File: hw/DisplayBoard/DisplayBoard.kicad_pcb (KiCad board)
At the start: 2 copper layers, 71.1 x 50.8 mm, 21 parts, among them Q1 2N3906, Q2 2N3906, Q3 2N3906, Q4 2N3906, U1 CA56-12EWA

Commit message: routed all traces
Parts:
- added J1: Conn_02x08_Odd_Even, Pin_Headers:Pin_Header_Straight_2x08_Pitch2.54mm, F.Cu at (58.4, 97.2)
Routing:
- net /AN3: track 0.00 -> 44.7 mm, vias 0 -> 1
- net Net-(R2-Pad1): track 0.00 -> 43.9 mm
- net /AN2: track 0.00 -> 43.2 mm, vias 0 -> 1
- net /AN1: track 0.00 -> 41.4 mm, vias 0 -> 1
- net /AN0: track 0.00 -> 39.8 mm
- net /VCC3: track 0.00 -> 39.5 mm
- net Net-(R1-Pad1): track 0.00 -> 39.4 mm
- net /VCC2: track 0.00 -> 38.2 mm
- net /VCC1: track 0.00 -> 35.2 mm
- net /VCC0: track 0.00 -> 31.5 mm
- net Net-(Q1-Pad3): track 0.00 -> 30.6 mm
- net Net-(R6-Pad1): track 0.00 -> 30.5 mm, vias 0 -> 1
- net Net-(Q3-Pad3): track 0.00 -> 30.1 mm
- net Net-(Q4-Pad3): track 0.00 -> 28.7 mm
- net Net-(R3-Pad1): track 0.00 -> 28.0 mm
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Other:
- board text added: "HexClock display board 0.1 11-May-2019 https://github.com/daveho/HexClock"

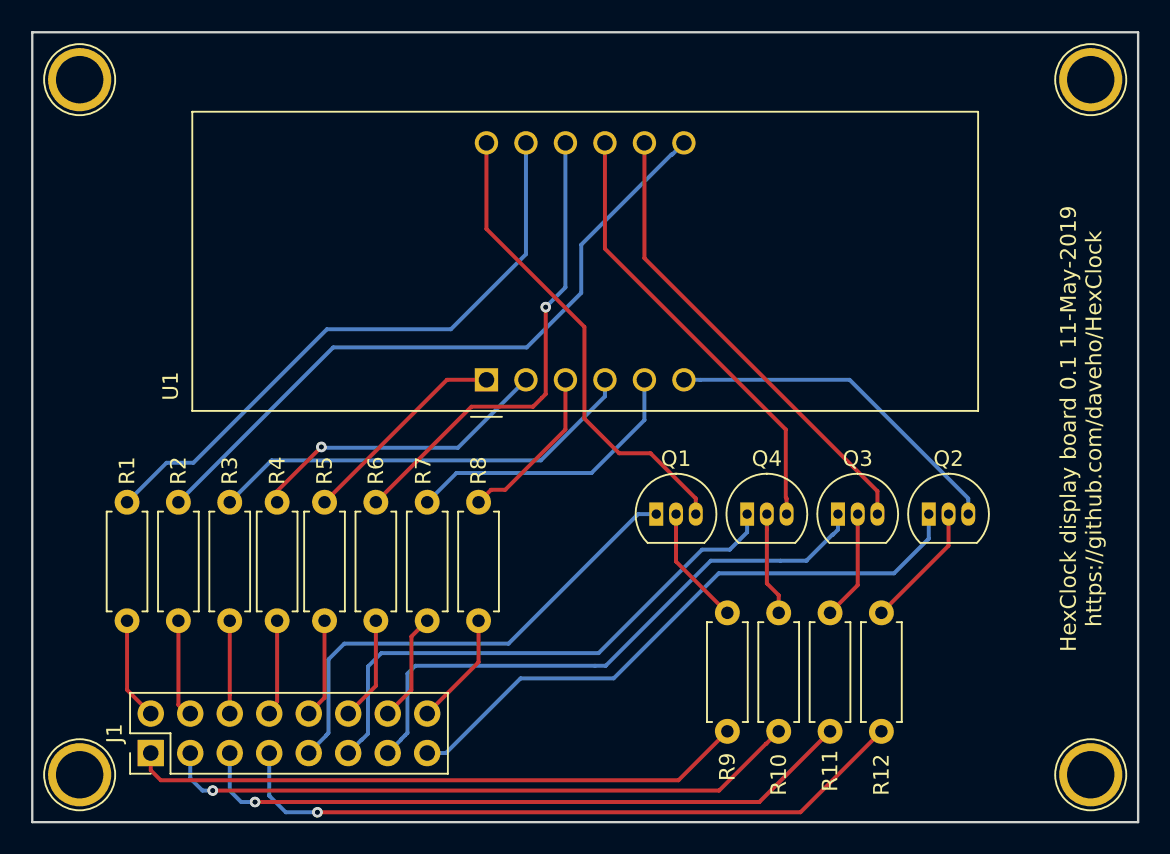
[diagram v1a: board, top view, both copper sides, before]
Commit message: copper pours on both copper layers
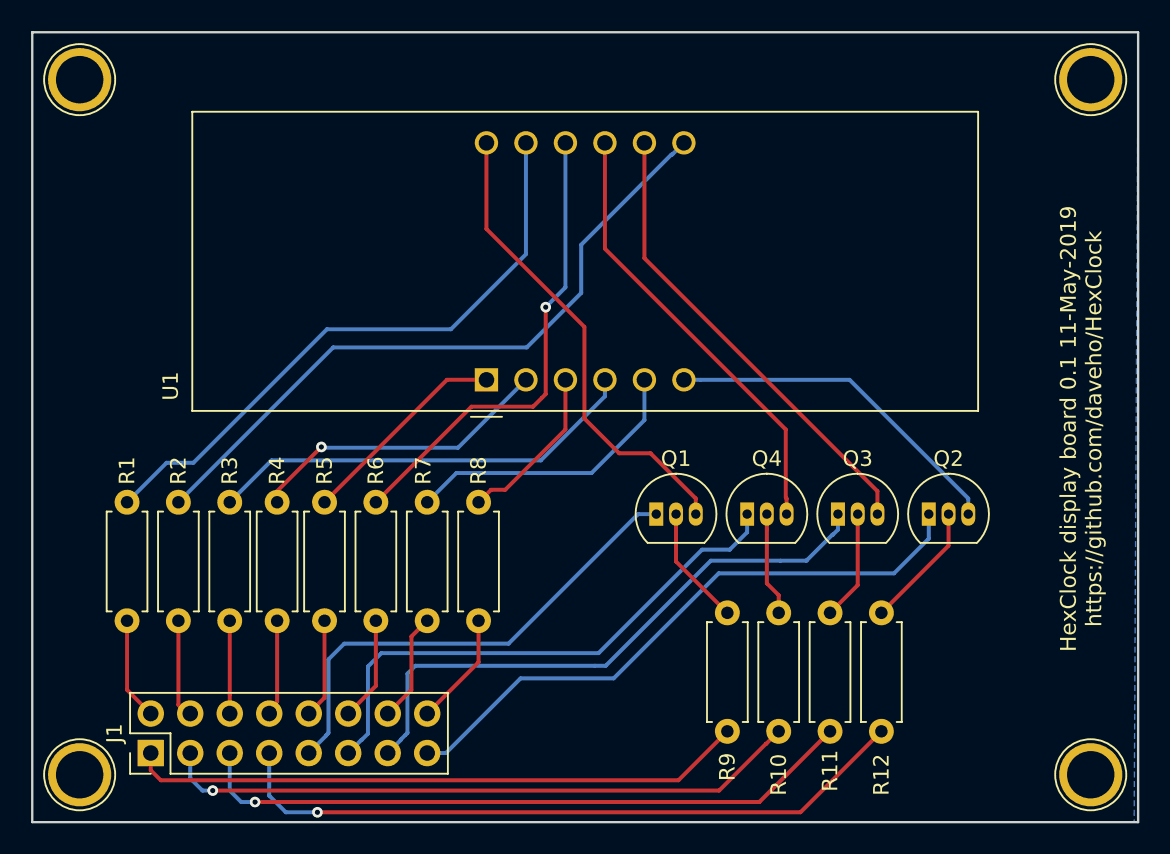
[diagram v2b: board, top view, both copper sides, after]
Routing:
- added copper zone on B.Cu, net (none)
- added copper zone on F.Cu, net (none)
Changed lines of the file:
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@@
   (segment (start 56.896 93.091) (end 56.896 88.646) (width 0.254) (layer F.Cu) (net 32))
   (segment (start 58.42 94.615) (end 56.896 93.091) (width 0.254) (layer F.Cu) (net 32))
+  (zone (net 0) (net_name "") (layer B.Cu) (hatch edge 0.508)
+    (connect_pads (clearance 0.508))
+    (min_thickness 0.254)
+    (fill yes (arc_segments 16) (thermal_gap 0.508) (thermal_bridge_width 0.508))
+    (polygon
+      (pts
+        (xy 50.8 50.8) (xy 121.92 50.8) (xy 121.666 101.6) (xy 50.8 101.6)
+      )
+    )
+  )
+  (zone (net 0) (net_name "") (layer F.Cu) (hatch edge 0.508)
+    (connect_pads (clearance 0.508))
+    (min_thickness 0.254)
+    (fill yes (arc_segments 16) (thermal_gap 0.508) (thermal_bridge_width 0.508))
+    (polygon
+      (pts
+        (xy 50.8 50.8) (xy 121.92 50.8) (xy 121.92 101.6) (xy 50.8 101.6)
+      )
+    )
+  )
 )
